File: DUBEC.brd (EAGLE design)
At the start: 40 x 21.4 mm, 71 parts

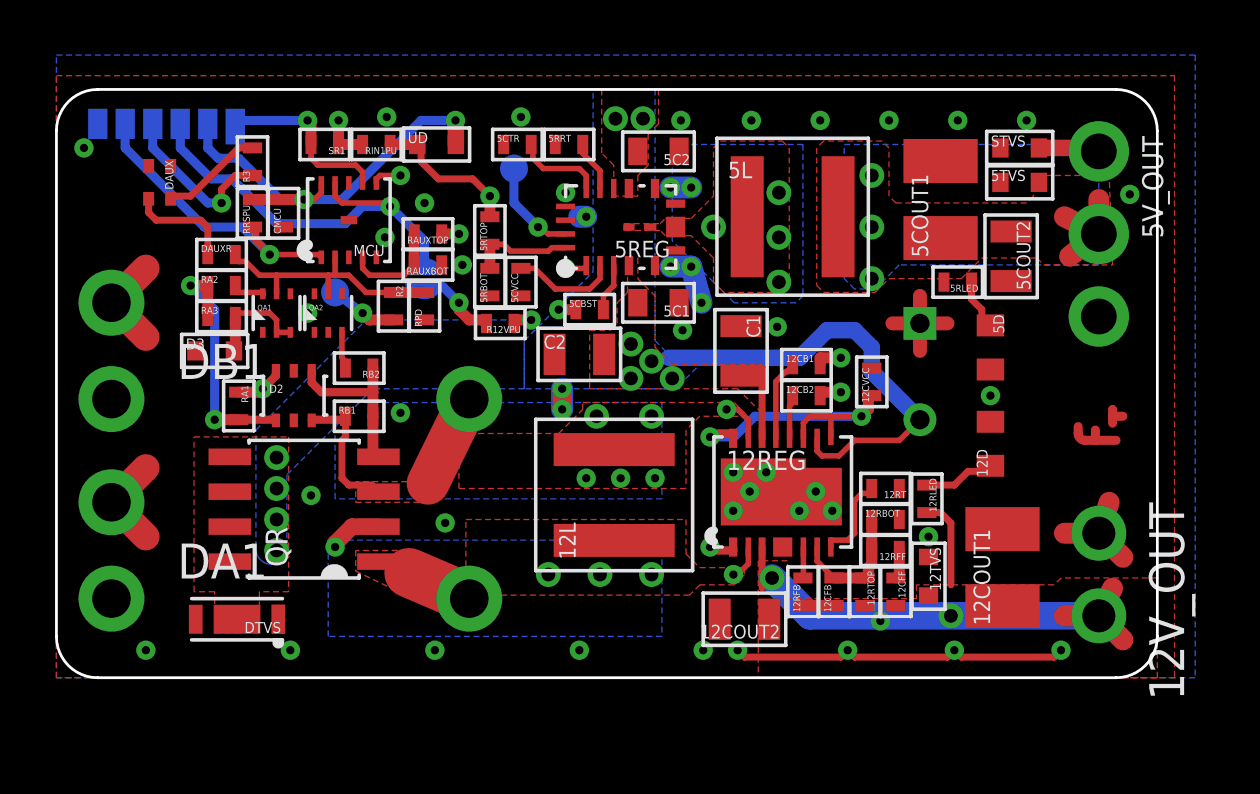
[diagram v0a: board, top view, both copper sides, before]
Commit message: Emblem to library; tweaks
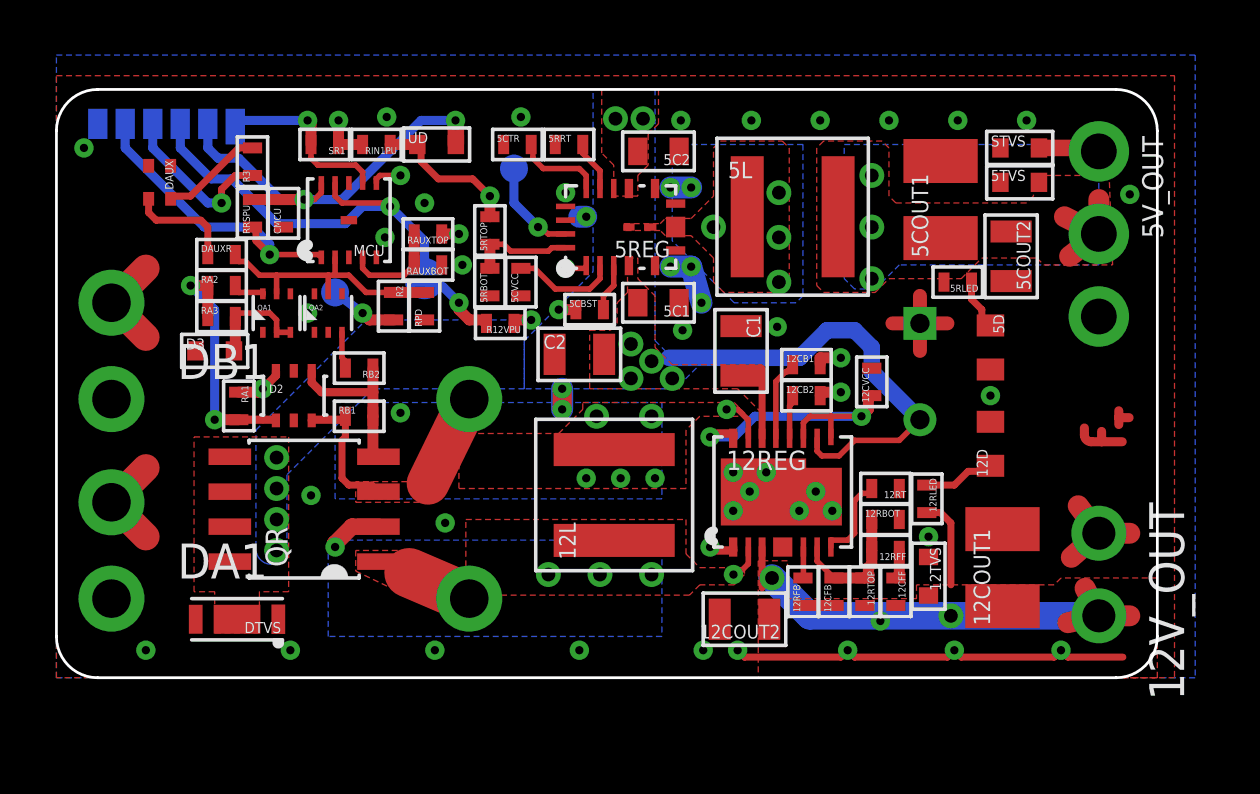
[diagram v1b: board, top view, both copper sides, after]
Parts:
- added U$1: (no value), dubec:TF-EMBLEM
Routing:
- net EMBLEM: track 2.98 -> 0.00 mm
- net GND: track 31.7 -> 34.1 mm
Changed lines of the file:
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@@
 <?xml version="1.0" encoding="utf-8"?>
 <!DOCTYPE eagle SYSTEM "eagle.dtd">
-<eagle version="7.4.0">
+<eagle version="7.5.0">
 <drawing>
 <settings>
@@
 <wire x1="1.5" y1="21.375" x2="0" y2="19.875" width="0.1" layer="20" curve="90"/>
 <wire x1="0" y1="19.875" x2="0" y2="1.5" width="0.1" layer="20"/>
-<text x="34.875" y="8.5" size="1.27" layer="107" font="vector" ratio="20" rot="SR90" align="top-center">12V</text>
-<text x="34.875" y="12.125" size="1.25" layer="107" font="vector" ratio="20" rot="R90" align="top-center">5V</text>
-<text x="2.625" y="17.875" size="1.27" layer="107" font="vector" ratio="20" rot="SR270" align="top-center">AUX</text>
+<text x="35" y="8.5" size="1.27" layer="107" font="vector" ratio="20" rot="SR90" align="top-center">12V</text>
+<text x="35" y="12.125" size="1.25" layer="107" font="vector" ratio="20" rot="R90" align="top-center">5V</text>
+<text x="2.75" y="17.875" size="1.27" layer="107" font="vector" ratio="20" rot="SR270" align="top-center">AUX</text>
 <text x="36.125" y="16.125" size="1.25" layer="22" font="vector" ratio="20" distance="30" rot="SMR270" align="bottom-center">+5V
 (3A)</text>
 <text x="36.125" y="19.125" size="1.25" layer="22" font="vector" ratio="20" rot="SMR270" align="bottom-center">S</text>
-<text x="36.125" y="13" size="1.25" layer="22" font="vector" ratio="20" rot="SMR270" align="bottom-center">-</text>
+<text x="37.875" y="11.5" size="1.25" layer="22" font="vector" ratio="20" rot="SMR270" align="center-left">-</text>
 <text x="29.75" y="19.625" size="2.8" layer="22" font="vector" ratio="20" rot="MR0" align="top-left">Super
 DUBEC</text>
@@
 <circle x="37.875" y="2.25" radius="1.125" width="0.254" layer="41"/>
 <circle x="2" y="10.125" radius="1.5" width="0.6" layer="41"/>
-<text x="16.625" y="19.5" size="0.8128" layer="22" font="vector" ratio="20" rot="MR0" align="bottom-center">5VPG</text>
-<text x="10.125" y="15" size="0.8128" layer="22" font="vector" ratio="20" rot="MR0" align="bottom-center">AUX</text>
+<text x="16.625" y="19.75" size="0.8128" layer="22" font="vector" ratio="20" rot="MR0" align="bottom-center">5VPG</text>
+<text x="10.125" y="15.25" size="0.8128" layer="22" font="vector" ratio="20" rot="MR0" align="bottom-center">AUX</text>
 <wire x1="26.01" y1="4.8" x2="26.765" y2="4.8" width="0.254" layer="41"/>
-<text x="3.75" y="4.75" size="1.25" layer="22" font="vector" ratio="20" rot="MR90" align="bottom-center">+MAIN-</text>
-<text x="3.75" y="11.875" size="1.25" layer="22" font="vector" ratio="20" rot="MR90" align="bottom-center">+AUX-</text>
+<text x="4" y="4.75" size="1.25" layer="22" font="vector" ratio="20" rot="MR90" align="bottom-center">+MAIN-</text>
+<text x="4" y="11.875" size="1.25" layer="22" font="vector" ratio="20" rot="MR90" align="bottom-center">+AUX-</text>
 <wire x1="38.125" y1="8" x2="39" y2="7.5" width="0.3302" layer="43"/>
 <wire x1="39" y1="7.5" x2="38.5" y2="8" width="0.3302" layer="43"/>
 <wire x1="38.5" y1="8" x2="39.25" y2="7.75" width="0.002540625" layer="43"/>
-<polygon width="0.381" layer="29">
-<vertex x="36.875" y="8.75"/>
-<vertex x="36.875" y="9.625" curve="-90"/>
-<vertex x="37.25" y="10"/>
-<vertex x="38.625" y="10" curve="-90"/>
-<vertex x="39" y="9.625"/>
-<vertex x="39" y="8.75" curve="-90"/>
-<vertex x="38.625" y="8.375"/>
-<vertex x="37.25" y="8.375" curve="-90"/>
-</polygon>
-<polygon width="0.381" layer="41">
-<vertex x="36.75" y="8.625"/>
-<vertex x="36.75" y="9.75" curve="-90"/>
-<vertex x="37.125" y="10.125"/>
-<vertex x="38.75" y="10.125" curve="-90"/>
-<vertex x="39.125" y="9.75"/>
-<vertex x="39.125" y="8.625" curve="-90"/>
-<vertex x="38.75" y="8.25"/>
-<vertex x="37.125" y="8.25" curve="-90"/>
-</polygon>
 <circle x="2" y="2.875" radius="1.5" width="0.6" layer="41"/>
 <circle x="15" y="2.875" radius="1.5" width="0.6" layer="41"/>
@@
 <rectangle x1="10.75" y1="16.125" x2="11.25" y2="16.75" layer="31"/>
 <rectangle x1="9.875" y1="16.125" x2="10.375" y2="16.75" layer="31"/>
-<text x="13.375" y="16.125" size="0.8128" layer="22" font="vector" ratio="20" rot="MR0" align="bottom-center">!12V</text>
-<text x="4" y="19" size="0.8128" layer="22" font="vector" ratio="20" rot="MR0" align="top-center">AVR ISP</text>
+<text x="13.375" y="16.375" size="0.8128" layer="22" font="vector" ratio="20" rot="MR0" align="bottom-center">!12V</text>
+<text x="4" y="18.875" size="0.8128" layer="22" font="vector" ratio="20" rot="MR0" align="top-center">AVR ISP</text>
 <text x="29.75" y="9" size="0.8128" layer="22" font="vector" ratio="20" rot="MR0">201x-xx-xx</text>
 <text x="32.375" y="6.375" size="1.25" layer="22" font="vector" ratio="20" rot="MR0">TURBOFUNCTION.com/fpv</text>
@@
 <attribute name="TEMP" value="±100ppm/°C" x="7.125" y="16.875" size="1.778" layer="27" rot="R90" display="off"/>
 </element>
+<element name="U$1" library="dubec" package="TF-EMBLEM" value="" x="38.125" y="9.125" rot="R90"/>
 </elements>
 <signals>
@@
 </polygon>
 <contactref element="12V_OUT" pad="1"/>
-<wire x1="37.875" y1="5.25" x2="38.25" y2="6.375" width="0.762" layer="1"/>
+<wire x1="37.875" y1="5.25" x2="37.125" y2="6.25" width="0.762" layer="1"/>
 <contactref element="RPD" pad="1"/>
 <contactref element="5D" pad="C"/>
-<wire x1="38.75" y1="4.375" x2="37.875" y2="5.25" width="0.762" layer="1"/>
+<wire x1="39" y1="5.25" x2="37.875" y2="5.25" width="0.762" layer="1"/>
 <via x="30.25" y="20.25" extent="1-16" drill="0.3"/>
 <via x="27.75" y="20.25" extent="1-16" drill="0.3"/>
@@
 <wire x1="18.375" y1="9.75" x2="18.375" y2="10.5" width="0.8" layer="16"/>
 <contactref element="12COUT1" pad="C"/>
-<wire x1="37.875" y1="5.25" x2="36.625" y2="5.25" width="0.762" layer="1"/>
+<wire x1="37.875" y1="5.25" x2="36.875" y2="4.375" width="0.762" layer="1"/>
 <via x="12" y="20.375" extent="1-16" drill="0.3"/>
 <via x="13.375" y="17.25" extent="1-16" drill="0.3"/>
@@
 <wire x1="32.875" y1="0.75" x2="36.25" y2="0.75" width="0.254" layer="1"/>
 <wire x1="36.25" y1="0.75" x2="36.5" y2="1" width="0.254" layer="1"/>
+<wire x1="36.5" y1="1" x2="36.75" y2="0.75" width="0.254" layer="1"/>
+<wire x1="36.75" y1="0.75" x2="38.75" y2="0.75" width="0.254" layer="1"/>
 </signal>
 <signal name="12V">
@@
 <wire x1="25.64" y1="4.75" x2="25.64" y2="3.265" width="0.254" layer="1"/>
 <via x="26" y="3.625" extent="1-16" drill="0.5"/>
-<wire x1="37.875" y1="2.25" x2="38.75" y2="1.375" width="0.762" layer="1"/>
-<wire x1="37.875" y1="2.25" x2="38.375" y2="3.25" width="0.762" layer="1"/>
+<wire x1="37.875" y1="2.25" x2="39" y2="2.25" width="0.762" layer="1"/>
+<wire x1="37.875" y1="2.25" x2="37.375" y2="3.25" width="0.762" layer="1"/>
 <via x="29.9375" y="2.0625" extent="1-16" drill="0.3"/>
 <contactref element="12COUT1" pad="A"/>
@@
 <wire x1="26" y1="3.625" x2="27.375" y2="2.25" width="1" layer="16"/>
 <wire x1="27.375" y1="2.25" x2="37.875" y2="2.25" width="1" layer="16"/>
-<wire x1="37.875" y1="2.25" x2="36.625" y2="2.25" width="0.762" layer="1"/>
+<wire x1="37.875" y1="2.25" x2="36.75" y2="2" width="0.762" layer="1"/>
 <wire x1="31.625" y1="6" x2="32.125" y2="6" width="0.254" layer="1"/>
 <wire x1="32.125" y1="6" x2="32.5" y2="5.625" width="0.254" layer="1"/>
@@
 <wire x1="2.5" y1="20.125" x2="2.5" y2="19.25" width="0.3302" layer="16"/>
 <wire x1="2.5" y1="19.25" x2="5.375" y2="16.375" width="0.3302" layer="16"/>
-<wire x1="5.375" y1="16.375" x2="6.75" y2="16.375" width="0.3302" layer="16"/>
-<wire x1="6.75" y1="16.375" x2="7.75" y2="15.375" width="0.3302" layer="16"/>
+<wire x1="5.375" y1="16.375" x2="7.125" y2="16.375" width="0.3302" layer="16"/>
+<wire x1="7.125" y1="16.375" x2="7.75" y2="15.75" width="0.3302" layer="16"/>
+<wire x1="7.75" y1="15.75" x2="7.75" y2="15.375" width="0.3302" layer="16"/>
 <contactref element="RRSPU" pad="1"/>
 <wire x1="7.125" y1="16.375" x2="7.25" y2="16.25" width="0.254" layer="1"/>
@@
 <wire x1="7.25" y1="15.875" x2="7.75" y2="15.375" width="0.254" layer="1"/>
 </signal>
-<signal name="EMBLEM">
-<wire x1="38.375" y1="9.5" x2="38.375" y2="9.75" width="0.3302" layer="1"/>
-<wire x1="38.375" y1="9.5" x2="38.75" y2="9.5" width="0.3302" layer="1"/>
-<wire x1="37.375" y1="8.625" x2="37.125" y2="8.875" width="0.3302" layer="1" curve="-90"/>
-<wire x1="37.125" y1="8.875" x2="37.125" y2="9.125" width="0.3302" layer="1"/>
-<wire x1="37.375" y1="8.625" x2="37.75" y2="8.625" width="0.3302" layer="1"/>
-<wire x1="37.75" y1="8.625" x2="38.5" y2="8.625" width="0.3302" layer="1"/>
-<wire x1="37.75" y1="8.625" x2="37.75" y2="9" width="0.3302" layer="1"/>
-<wire x1="38.375" y1="9.25" x2="38.375" y2="9.5" width="0.3302" layer="1"/>
-<wire x1="38.5" y1="8.625" x2="38.375" y2="9.25" width="0" layer="19" extent="1-1"/>
-</signal>
 <signal name="N$2">

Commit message: AUX divider update (due to non-stock)
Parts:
- RAUXBOT: value RES3.16K_16 -> RES2.74K_16
- RAUXTOP: value RES20K_16 -> RES17.8K_16
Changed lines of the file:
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@@
 <attribute name="EURO" value="4.06/10" x="31.6875" y="3.6875" size="1.778" layer="27" rot="R270" display="off"/>
 </element>
-<element name="RAUXTOP" library="dubec" package="0402" value="RES20K_16" x="13.5" y="16.125" rot="R180">
+<element name="RAUXTOP" library="dubec" package="0402" value="RES17.8K_16" x="13.5" y="16.125" rot="R180">
 <attribute name="MANUFACTURER" value="Vishay Dale" x="13.5" y="16.125" size="1.778" layer="27" rot="R180" display="off"/>
-<attribute name="MFG_PART_#" value="CRCW040220K0FKED" x="13.5" y="16.125" size="1.778" layer="27" rot="R180" display="off"/>
+<attribute name="MFG_PART_#" value="CRCW040217K8FKED" x="13.5" y="16.125" size="1.778" layer="27" rot="R180" display="off"/>
 <attribute name="TOLERANCE" value="±1%" x="13.5" y="16.125" size="1.778" layer="27" rot="R180" display="off"/>
 <attribute name="TEMP" value="±100ppm/°C" x="13.5" y="16.125" size="1.778" layer="27" rot="R180" display="off"/>
-<attribute name="DIGIKEY_PART_#" value="541-20.0KLCT-ND" x="13.5" y="16.125" size="1.778" layer="27" rot="R180" display="off"/>
+<attribute name="DIGIKEY_PART_#" value="541-17.8KLCT-ND" x="13.5" y="16.125" size="1.778" layer="27" rot="R180" display="off"/>
 <attribute name="EURO" value="2.01/50" x="13.5" y="16.125" size="1.778" layer="27" rot="R180" display="off"/>
 </element>
-<element name="RAUXBOT" library="dubec" package="0402" value="RES3.16K_16" x="13.5" y="15" rot="R180">
-<attribute name="DIGIKEY_PART_#" value="541-3.16KLCT-ND" x="13.5" y="15" size="1.778" layer="27" rot="R180" display="off"/>
+<element name="RAUXBOT" library="dubec" package="0402" value="RES2.74K_16" x="13.5" y="15" rot="R180">
+<attribute name="DIGIKEY_PART_#" value="541-2.74KLCT-ND" x="13.5" y="15" size="1.778" layer="27" rot="R180" display="off"/>
 <attribute name="MANUFACTURER" value="Vishay Dale" x="13.5" y="15" size="1.778" layer="27" rot="R180" display="off"/>
-<attribute name="MFG_PART_#" value="CRCW04023K16FKED" x="13.5" y="15" size="1.778" layer="27" rot="R180" display="off"/>
+<attribute name="MFG_PART_#" value="CRCW04022K74FKED" x="13.5" y="15" size="1.778" layer="27" rot="R180" display="off"/>
 <attribute name="TOLERANCE" value="±1%" x="13.5" y="15" size="1.778" layer="27" rot="R180" display="off"/>
 <attribute name="TEMP" value="±100ppm/°C" x="13.5" y="15" size="1.778" layer="27" rot="R180" display="off"/>
-<attribute name="EURO" value="2.01/50" x="13.5" y="15" size="1.778" layer="27" rot="R180" display="off"/>
 </element>
 <element name="CMCU" library="dubec" package="0402" value="" x="8.25" y="16.875" rot="R90">
